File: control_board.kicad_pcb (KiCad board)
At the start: 2 copper layers, 100 x 100 mm, 49 parts, among them J1 Servo_1_Conn, J10 LED_2_Conn, J11 LED_3_Conn, J12 LED_4_Conn, J13 Raspberry_Pi_Conn, J14 DC_Power_Header, J15 USB_Power_Jumper, J16 Jack-DC, J17 Herkulex Conn, J2 Servo_2_Conn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

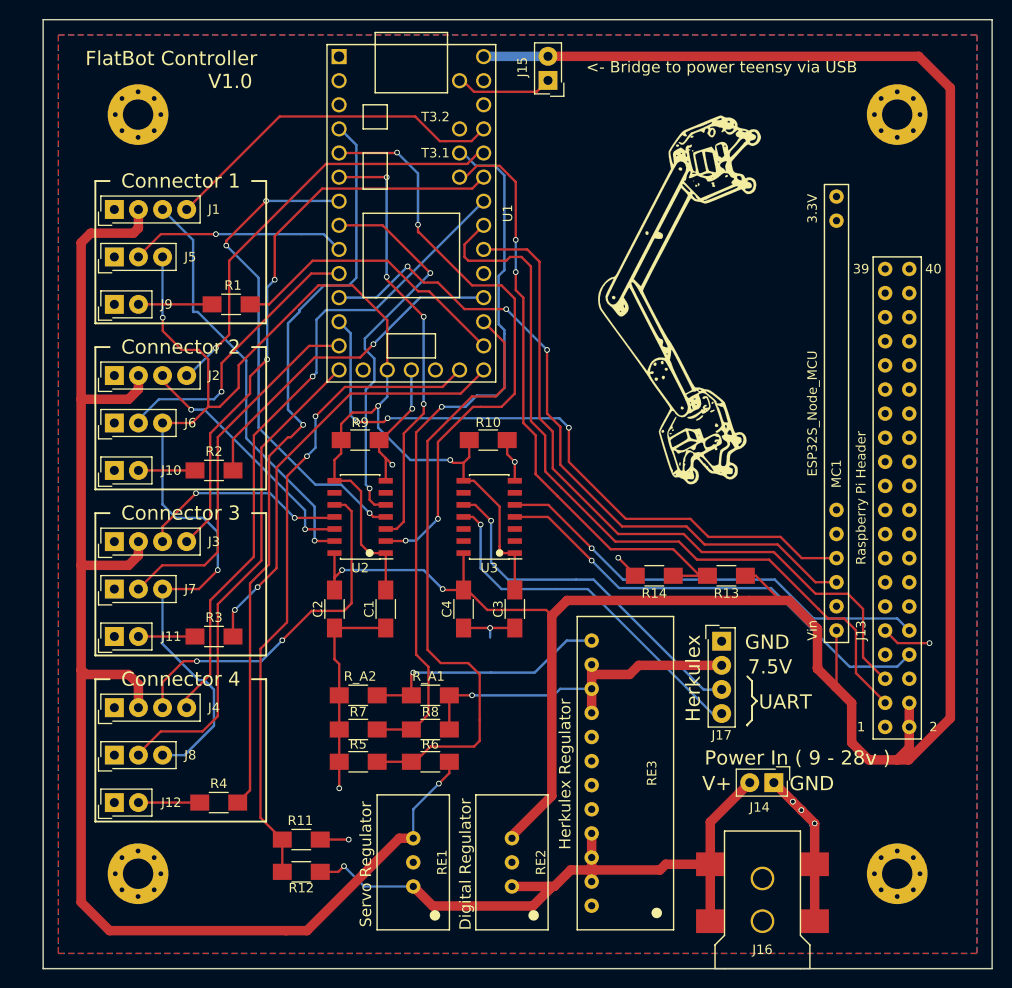
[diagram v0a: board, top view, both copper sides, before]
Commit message: Added resistor values, correct 7.5V reg enable pin and output cap
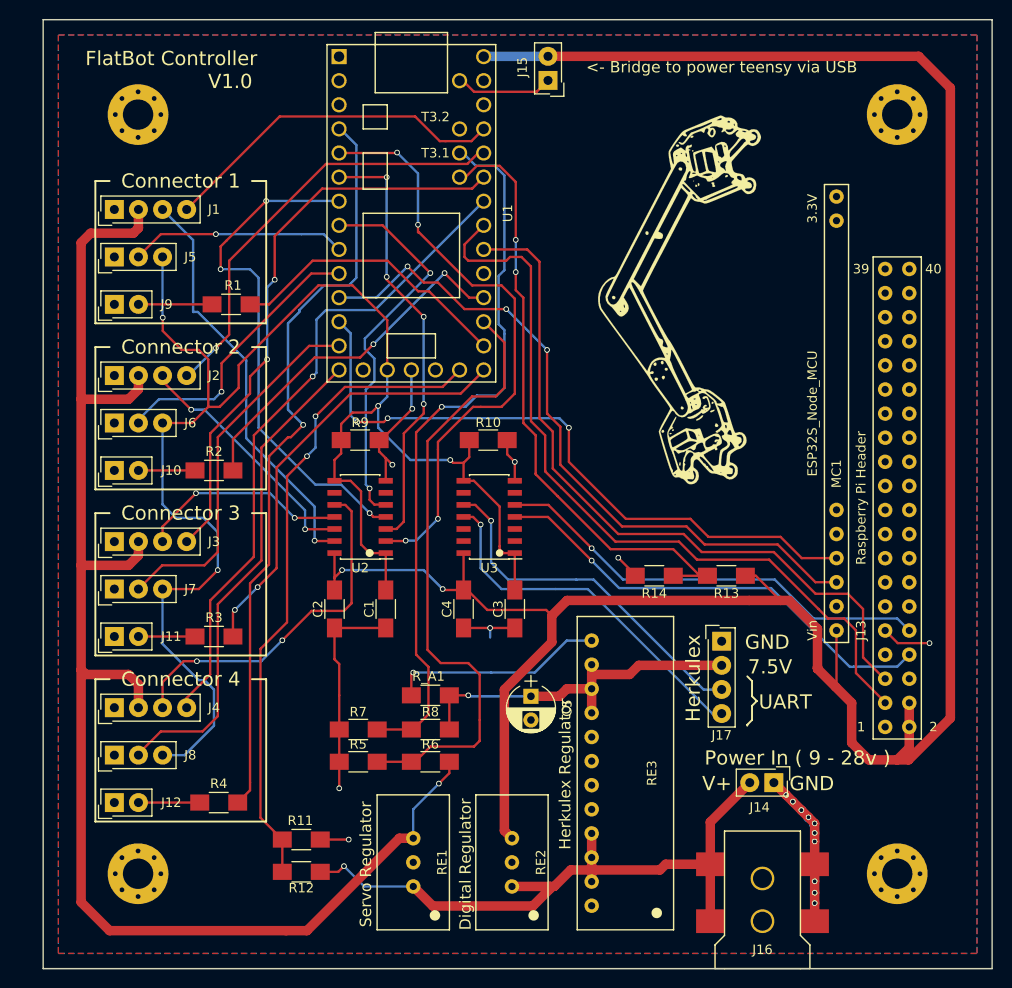
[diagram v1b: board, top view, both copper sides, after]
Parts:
- removed R_A2: R, Resistors_SMD:R_1206_HandSoldering
- added C5: CP 100uF, Capacitors_THT:CP_Radial_D5.0mm_P2.50mm, F.Cu at (141.4, 121.3)
- C1, C2, C3, C4: value C -> C 100nF
- R1, R2, R3, R4: value R220 -> R 220
- R10, R9: value R220 -> R 10k
- R11, R14, R5, R7: value R -> R 100k
- R12: value R -> R 750k
- R13, R6: value R -> R 62k
- R8: value R -> R 150k
- R_A1: value R -> R 15k
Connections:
- RE3 pad 1: GND -> /5V_Digital
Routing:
- net Net-(RE3-Pad5): track 26.3 -> 22.7 mm
- net /Servo_3_PWM: track 52.0 -> 54.3 mm
- net /LED_2: track 35.9 -> 38.0 mm, vias 1 -> 2
- net /5V_Digital: track 249.5 -> 250.4 mm
- net GND: track 75.6 -> 75.7 mm, vias 11 -> 18
